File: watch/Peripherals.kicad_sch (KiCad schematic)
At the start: 30 parts, among them IC501 APDS-9306-065, IC502 BMI270, IC503 LIS2MDLTR, IC504 BMP581, IC505 DRV2603RUNT, IC506 PCA9306JK, IC507 RV-8263-C8, M501 Vibrator DC Motor, X509 Motor

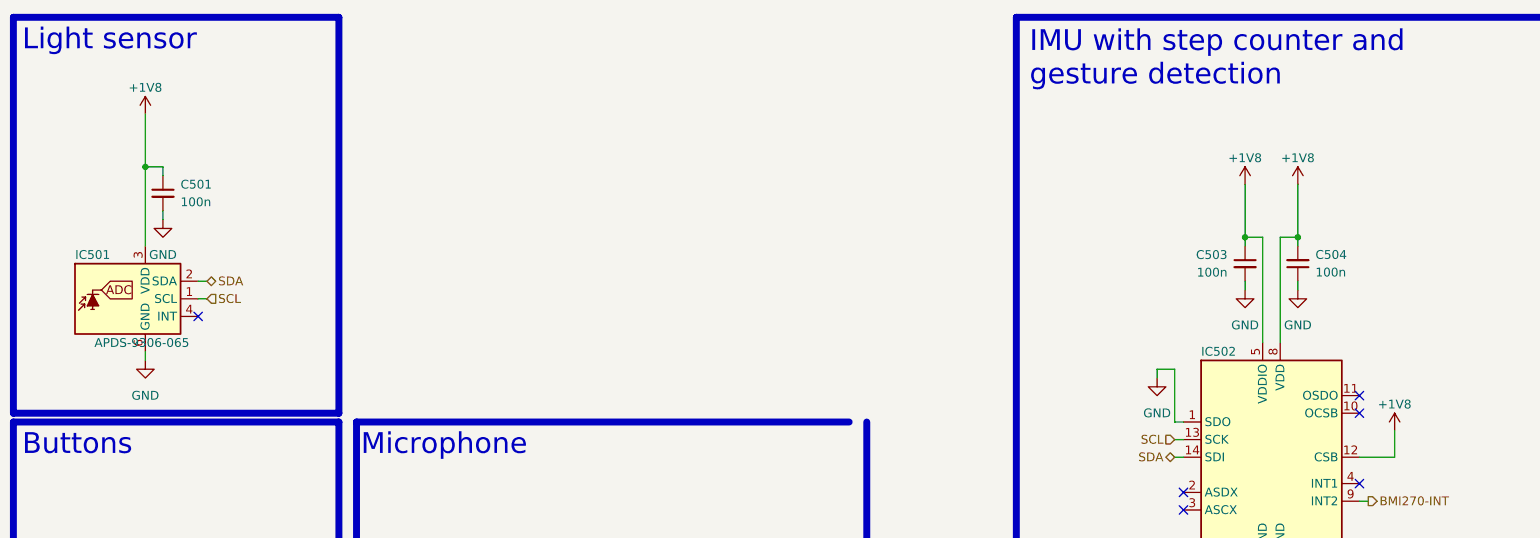
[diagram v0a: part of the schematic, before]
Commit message: Bug: Issue #14
- Change 3V0 to 3V3 to prevent flickering display

Closes: #14

Signed-off-by: Daniel Kampert <DanielKampert@kampis-elektroecke.de>
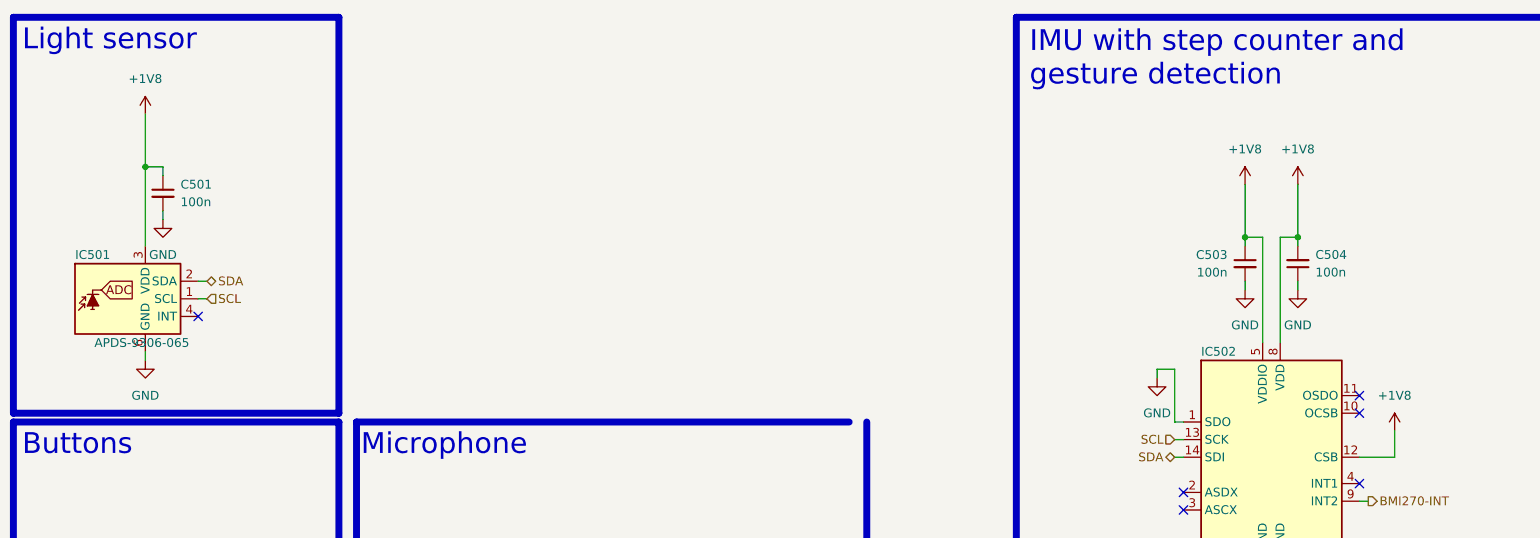
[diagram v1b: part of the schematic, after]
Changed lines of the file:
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@@
 		(dnp no)
 		(fields_autoplaced yes)
-		(property "Reference" "#PWR0530"
+		(property "Reference" "#PWR530"
 			(at 274.32 39.37 0)
 			(effects
@@
 			(project "Dev-Kit"
 				(path "/d5742f03-3b1a-42e5-a384-018bd4b919aa/c5103ceb-5325-4a84-a025-9638a412984e/82af773f-8c39-43b9-baa2-3658da6c8bb2"
-					(reference "#PWR0530")
+					(reference "#PWR530")
 					(unit 1)
 				)
@@
 		(dnp no)
 		(fields_autoplaced yes)
-		(property "Reference" "#PWR0533"
+		(property "Reference" "#PWR533"
 			(at 313.69 120.65 0)
 			(effects
@@
 			(project "ZSWatch-Watch-DevKit"
 				(path "/d5742f03-3b1a-42e5-a384-018bd4b919aa/c5103ceb-5325-4a84-a025-9638a412984e/82af773f-8c39-43b9-baa2-3658da6c8bb2"
-					(reference "#PWR0533")
+					(reference "#PWR533")
 					(unit 1)
 				)
@@
 		(dnp no)
 		(fields_autoplaced yes)
-		(property "Reference" "#PWR0532"
+		(property "Reference" "#PWR532"
 			(at 287.02 76.2 0)
 			(effects
@@
 			(project "Dev-Kit"
 				(path "/d5742f03-3b1a-42e5-a384-018bd4b919aa/c5103ceb-5325-4a84-a025-9638a412984e/82af773f-8c39-43b9-baa2-3658da6c8bb2"
-					(reference "#PWR0532")
+					(reference "#PWR532")
 					(unit 1)
 				)
@@
 		(dnp no)
 		(fields_autoplaced yes)
-		(property "Reference" "#PWR0602"
+		(property "Reference" "#PWR602"
 			(at 199.39 41.91 0)
 			(effects
@@
 		)
 		(property "Value" "+1V8"
-			(at 199.39 34.29 0)
+			(at 199.39 33.02 0)
 			(effects
 				(font
@@
 			(project "ZSWatch-Watch"
 				(path "/d5742f03-3b1a-42e5-a384-018bd4b919aa/c5103ceb-5325-4a84-a025-9638a412984e/82af773f-8c39-43b9-baa2-3658da6c8bb2"
-					(reference "#PWR0602")
+					(reference "#PWR602")
 					(unit 1)
 				)
@@
 		(dnp no)
 		(fields_autoplaced yes)
-		(property "Reference" "#PWR0537"
+		(property "Reference" "#PWR537"
 			(at 341.63 120.65 0)
 			(effects
@@
 			(project "Watch-DK"
 				(path "/d5742f03-3b1a-42e5-a384-018bd4b919aa/c5103ceb-5325-4a84-a025-9638a412984e/82af773f-8c39-43b9-baa2-3658da6c8bb2"
-					(reference "#PWR0537")
+					(reference "#PWR537")
 					(unit 1)
 				)
@@
 		(dnp no)
 		(fields_autoplaced yes)
-		(property "Reference" "#PWR0526"
+		(property "Reference" "#PWR526"
 			(at 266.7 39.37 0)
 			(effects
@@
 			(project "Dev-Kit"
 				(path "/d5742f03-3b1a-42e5-a384-018bd4b919aa/c5103ceb-5325-4a84-a025-9638a412984e/82af773f-8c39-43b9-baa2-3658da6c8bb2"
-					(reference "#PWR0526")
+					(reference "#PWR526")
 					(unit 1)
 				)
@@
 		(dnp no)
 		(fields_autoplaced yes)
-		(property "Reference" "#PWR0529"
+		(property "Reference" "#PWR529"
 			(at 265.43 128.27 0)
 			(effects
@@
 			(project "Dev-Kit"
 				(path "/d5742f03-3b1a-42e5-a384-018bd4b919aa/c5103ceb-5325-4a84-a025-9638a412984e/82af773f-8c39-43b9-baa2-3658da6c8bb2"
-					(reference "#PWR0529")
+					(reference "#PWR529")
 					(unit 1)
 				)
@@
 		(dnp no)
 		(fields_autoplaced yes)
-		(property "Reference" "#PWR0521"
+		(property "Reference" "#PWR521"
 			(at 256.54 76.2 0)
 			(effects
@@
 			(project "Dev-Kit"
 				(path "/d5742f03-3b1a-42e5-a384-018bd4b919aa/c5103ceb-5325-4a84-a025-9638a412984e/82af773f-8c39-43b9-baa2-3658da6c8bb2"
-					(reference "#PWR0521")
+					(reference "#PWR521")
 					(unit 1)
 				)
@@
 		(dnp no)
 		(fields_autoplaced yes)
-		(property "Reference" "#PWR0513"
+		(property "Reference" "#PWR513"
 			(at 191.77 41.91 0)
 			(effects
@@
 		)
 		(property "Value" "+1V8"
-			(at 191.77 34.29 0)
+			(at 191.77 33.02 0)
 			(effects
 				(font
@@
 			(project "Dev-Kit"
 				(path "/d5742f03-3b1a-42e5-a384-018bd4b919aa/c5103ceb-5325-4a84-a025-9638a412984e/82af773f-8c39-43b9-baa2-3658da6c8bb2"
-					(reference "#PWR0513")
+					(reference "#PWR513")
 					(unit 1)
 				)
@@
 		(dnp no)
 		(fields_autoplaced yes)
-		(property "Reference" "#PWR0502"
+		(property "Reference" "#PWR502"
 			(at 33.02 31.75 0)
 			(effects
@@
 		)
 		(property "Value" "+1V8"
-			(at 33.02 24.13 0)
+			(at 33.02 22.86 0)
 			(effects
 				(font
@@
 			(project "Dev-Kit"
 				(path "/d5742f03-3b1a-42e5-a384-018bd4b919aa/c5103ceb-5325-4a84-a025-9638a412984e/82af773f-8c39-43b9-baa2-3658da6c8bb2"
-					(reference "#PWR0502")
+					(reference "#PWR502")
 					(unit 1)
 				)
@@
 		(dnp no)
 		(fields_autoplaced yes)
-		(property "Reference" "#PWR0519"
+		(property "Reference" "#PWR519"
 			(at 220.98 161.29 0)
 			(effects
@@
 			(project "Dev-Kit"
 				(path "/d5742f03-3b1a-42e5-a384-018bd4b919aa/c5103ceb-5325-4a84-a025-9638a412984e/82af773f-8c39-43b9-baa2-3658da6c8bb2"
-					(reference "#PWR0519")
+					(reference "#PWR519")
 					(unit 1)
 				)
@@
 		(dnp no)
 		(fields_autoplaced yes)
-		(property "Reference" "#PWR0518"
+		(property "Reference" "#PWR518"
 			(at 213.36 77.47 0)
 			(effects
@@
 		)
 		(property "Value" "+1V8"
-			(at 213.36 69.85 0)
+			(at 213.36 68.58 0)
 			(effects
 				(font
@@
 			(project "Dev-Kit"
 				(path "/d5742f03-3b1a-42e5-a384-018bd4b919aa/c5103ceb-5325-4a84-a025-9638a412984e/82af773f-8c39-43b9-baa2-3658da6c8bb2"
-					(reference "#PWR0518")
+					(reference "#PWR518")
 					(unit 1)
 				)
@@
 		(dnp no)
 		(fields_autoplaced yes)
-		(property "Reference" "#PWR0522"
+		(property "Reference" "#PWR522"
 			(at 257.81 128.27 0)
 			(effects
@@
 			(project "Dev-Kit"
 				(path "/d5742f03-3b1a-42e5-a384-018bd4b919aa/c5103ceb-5325-4a84-a025-9638a412984e/82af773f-8c39-43b9-baa2-3658da6c8bb2"
-					(reference "#PWR0522")
+					(reference "#PWR522")
 					(unit 1)
 				)
